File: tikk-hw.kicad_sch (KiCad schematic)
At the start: 148 parts, among them J1 51281-0598, P6 ZX-SH1.0-4PWT, SW1 TS24CA, SW2 TS24CA, U1 IS31FL3731-QFLS2-TR, U2 LIS2DH12TR, U3 Tenstar nRF52840, U4 CP6208DTR(XBLW), U5 TMP102AIDRLR, U6 CP6208DTR(XBLW)

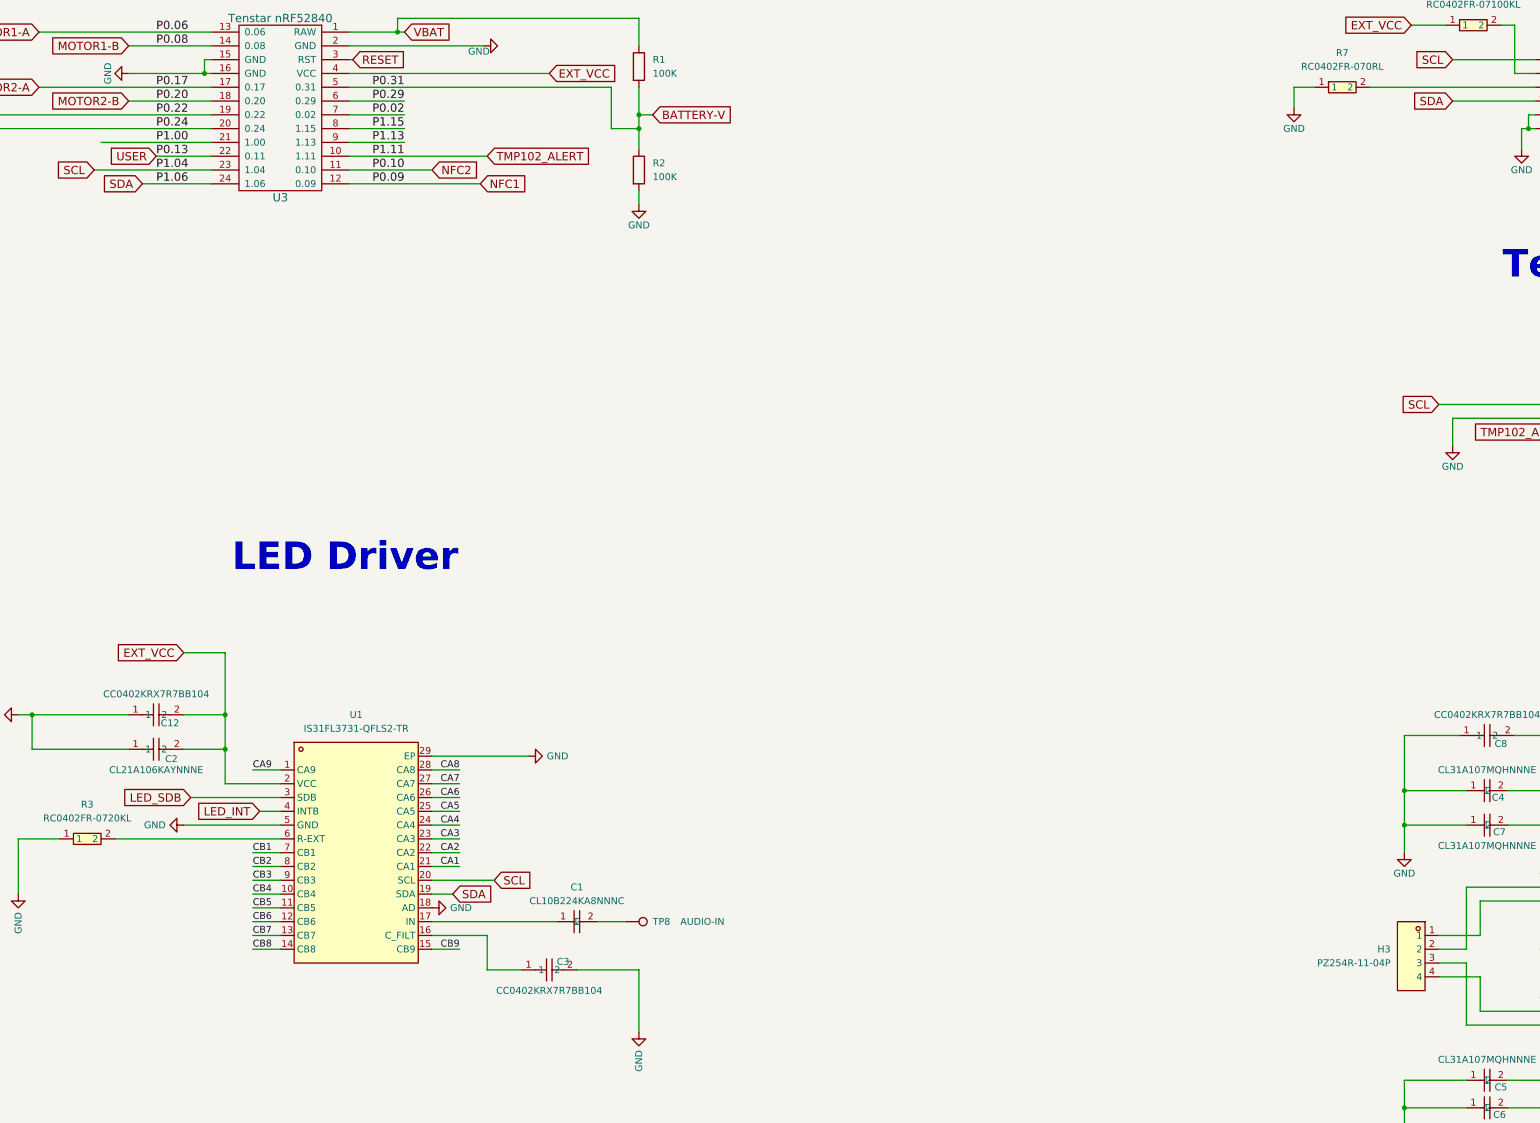
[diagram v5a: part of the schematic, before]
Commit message: Removed all initial DRC violations
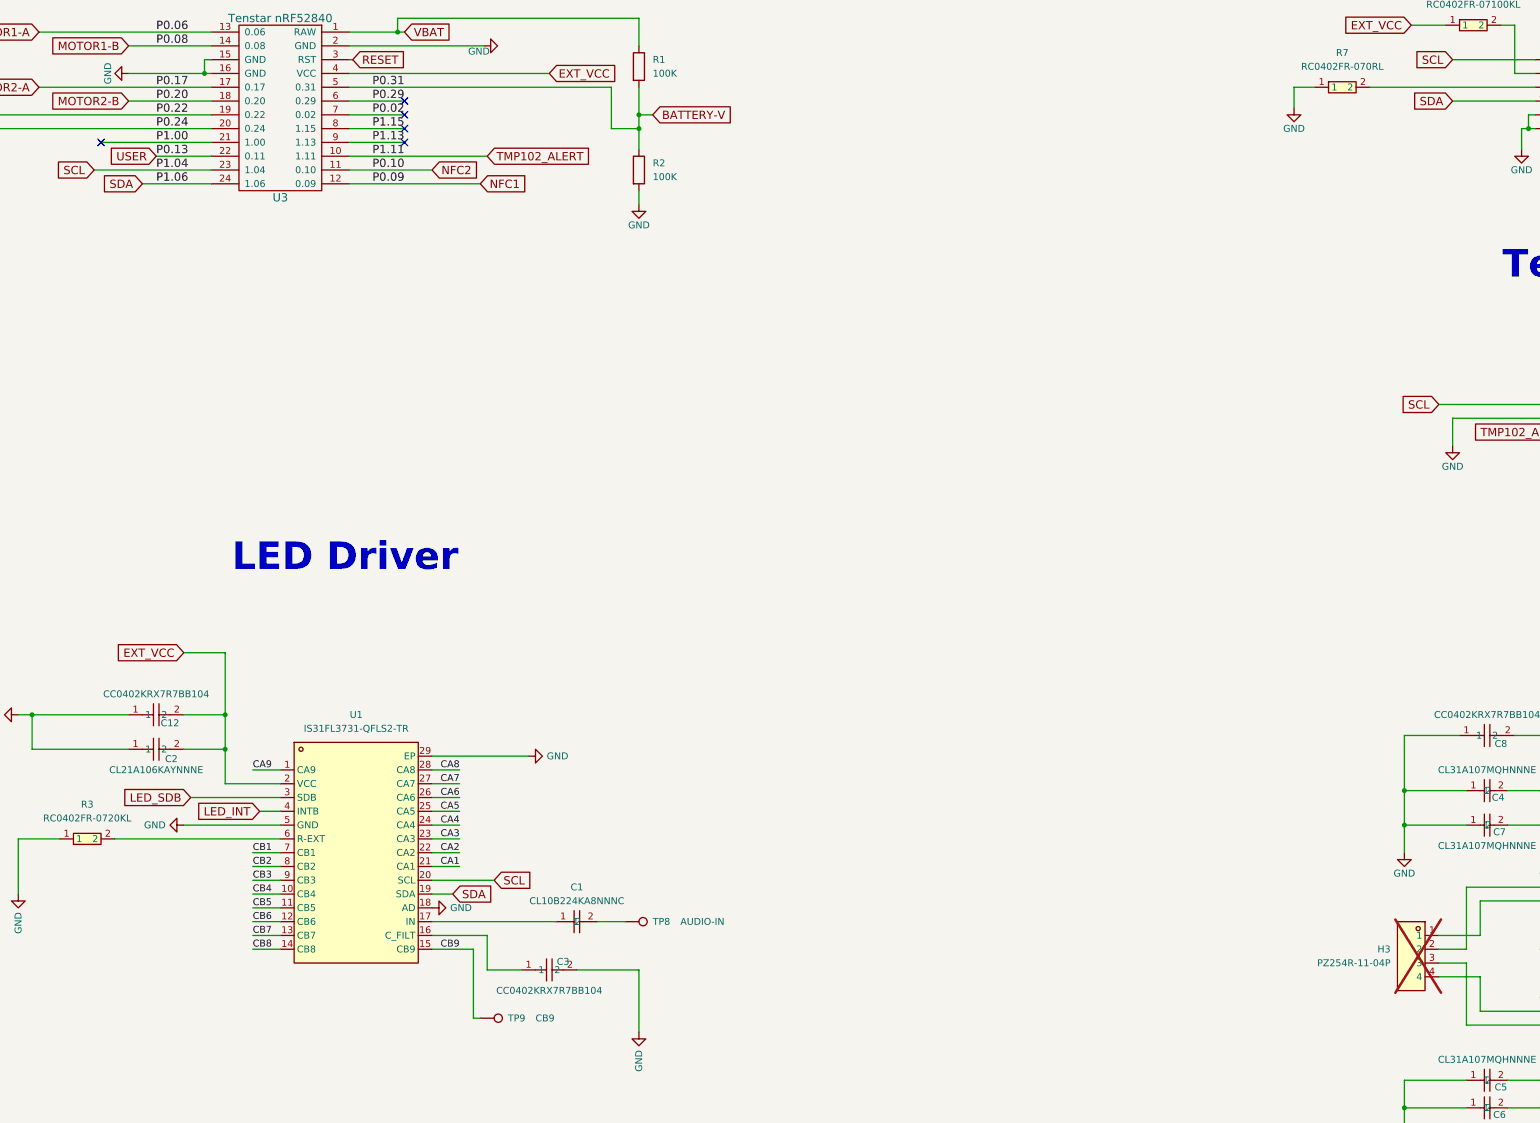
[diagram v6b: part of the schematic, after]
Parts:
- added TP9: CB9, TestPoint:TestPoint_Pad_D1.0mm, symbol Connector:TestPoint
- H3: now not fitted
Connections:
- net CB9: now also TP9.1
- no-connect marks 4 -> 9
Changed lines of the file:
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@@
 	)
 	(no_connect
+		(at 237.49 55.88)
+	)
+	(no_connect
+		(at 237.49 50.8)
+	)
+	(no_connect
 		(at 492.76 195.58)
 	)
 	(no_connect
+		(at 237.49 53.34)
+	)
+	(no_connect
 		(at 77.47 247.65)
 	)
@@
 		(at 77.47 250.19)
 	)
+	(no_connect
+		(at 181.61 55.88)
+	)
+	(no_connect
+		(at 237.49 48.26)
+	)
 	(wire
 		(pts
@@
 	(wire
 		(pts
+			(xy 250.19 204.47) (xy 250.19 217.17)
+		)
+		(stroke
+			(width 0)
+			(type default)
+		)
+	)
+	(wire
+		(pts
 			(xy 474.98 238.76) (xy 480.06 238.76)
 		)
@@
 	(wire
 		(pts
-			(xy 242.57 204.47) (xy 247.65 204.47)
+			(xy 242.57 204.47) (xy 250.19 204.47)
 		)
 		(stroke
@@
 	(wire
 		(pts
+			(xy 250.19 217.17) (xy 251.46 217.17)
+		)
+		(stroke
+			(width 0)
+			(type default)
+		)
+	)
+	(wire
+		(pts
 			(xy 140.97 297.18) (xy 140.97 311.15)
 		)
@@
 		(in_bom yes)
 		(on_board yes)
-		(dnp no)
+		(dnp yes)
 		(property "Reference" "H3"
 			(at 419.1 204.4699 0)
@@
 					(unit 1)
 				)
+			)
+		)
+	)
+	(symbol
+		(lib_id "Connector:TestPoint")
+		(at 251.46 217.17 270)
+		(unit 1)
+		(exclude_from_sim no)
+		(in_bom yes)
+		(on_board yes)
+		(dnp no)
+		(property "Reference" "TP9"
+			(at 256.54 217.17 90)
+			(effects
+				(font
+					(size 1.27 1.27)
+				)
+				(justify left)
+			)
+		)
+		(property "Value" "CB9"
+			(at 261.62 217.17 90)
+			(effects
+				(font
+					(size 1.27 1.27)
+				)
+				(justify left)
+			)
+		)
+		(property "Footprint" "TestPoint:TestPoint_Pad_D1.0mm"
+			(at 251.46 222.25 0)
+			(effects
+				(font
+					(size 1.27 1.27)
+				)
+				(hide yes)
+			)
+		)
+		(property "Datasheet" "~"
+			(at 251.46 222.25 0)
+			(effects
+				(font
+					(size 1.27 1.27)
+				)
+				(hide yes)
+			)
+		)
+		(property "Description" "test point"
+			(at 251.46 217.17 0)
+			(effects
+				(font
+					(size 1.27 1.27)
+				)
+				(hide yes)
+			)
+		)
+		(pin "1"
+		)
+		(instances
+			(project "tikk-hw"
+				(path "/3d32aeaf-a681-4c47-a6d3-68ef8c82b0dd"
+					(reference "TP9")
+					(unit 1)
+				)

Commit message: updated to add silkscreen qr code area and optimized component info
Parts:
- H1, H2, JP1, TP1, TP2, TP3, TP4, TP5, TP6, TP7, TP8, TP9, U3: now not fitted
- R1, R2: value 100K -> RC0402FR-07100KL
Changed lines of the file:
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@@
 			)
 		)
-		(property "Value" "100K"
+		(property "Value" "RC0402FR-07100KL"
 			(at 283.21 62.2299 0)
 			(effects
@@
 		(in_bom yes)
 		(on_board yes)
-		(dnp no)
+		(dnp yes)
 		(property "Reference" "TP8"
 			(at 283.21 199.39 90)
@@
 		(in_bom yes)
 		(on_board yes)
-		(dnp no)
+		(dnp yes)
 		(property "Reference" "TP4"
 			(at 66.04 53.34 90)
@@
 		(in_bom yes)
 		(on_board yes)
-		(dnp no)
+		(dnp yes)
 		(property "Reference" "TP1"
 			(at 65.786 45.72 90)
@@
 		(in_bom yes)
 		(on_board yes)
-		(dnp no)
+		(dnp yes)
 		(property "Reference" "TP3"
 			(at 65.786 50.8 90)
@@
 		(in_bom no)
 		(on_board yes)
-		(dnp no)
+		(dnp yes)
 		(fields_autoplaced yes)
 		(property "Reference" "H1"
@@
 		(in_bom yes)
 		(on_board yes)
-		(dnp no)
+		(dnp yes)
 		(property "Reference" "U3"
 			(at 214.63 66.04 0)
@@
 		(in_bom yes)
 		(on_board yes)
-		(dnp no)
+		(dnp yes)
 		(property "Reference" "TP5"
 			(at 94.996 55.88 90)
@@
 			)
 		)
-		(property "Value" "100K"
+		(property "Value" "RC0402FR-07100KL"
 			(at 283.21 43.1799 0)
 			(effects
@@
 		(in_bom yes)
 		(on_board yes)
-		(dnp no)
+		(dnp yes)
 		(property "Reference" "TP9"
 			(at 256.54 217.17 90)
@@
 		(in_bom yes)
 		(on_board yes)
-		(dnp no)
+		(dnp yes)
 		(property "Reference" "TP7"
 			(at 82.55 250.19 90)
@@
 		(in_bom no)
 		(on_board yes)
-		(dnp no)
+		(dnp yes)
 		(fields_autoplaced yes)
 		(property "Reference" "H2"
@@
 		(in_bom yes)
 		(on_board yes)
-		(dnp no)
+		(dnp yes)
 		(property "Reference" "TP6"
 			(at 82.55 247.65 90)
@@
 		(in_bom no)
 		(on_board yes)
-		(dnp no)
+		(dnp yes)
 		(fields_autoplaced yes)
 		(property "Reference" "JP1"
@@
 		(in_bom yes)
 		(on_board yes)
-		(dnp no)
+		(dnp yes)
 		(property "Reference" "TP2"
 			(at 95.25 48.26 90)

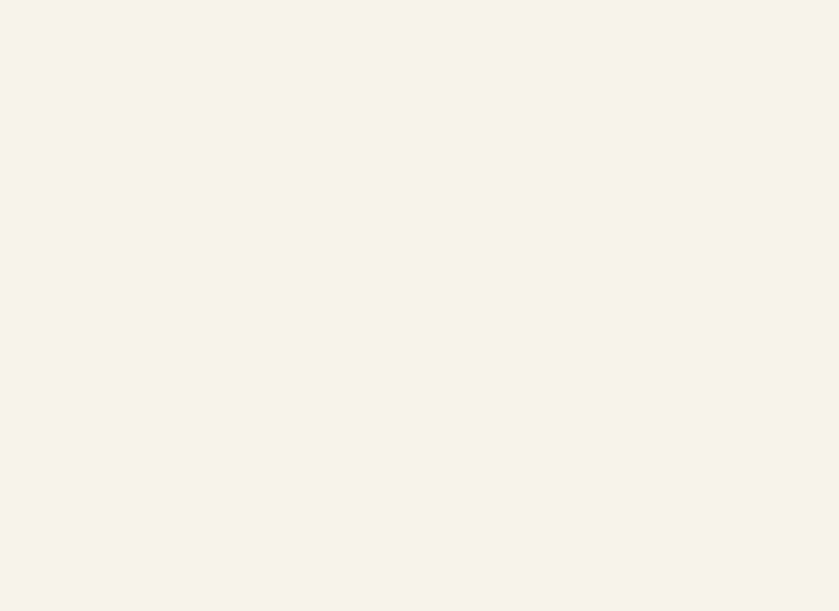
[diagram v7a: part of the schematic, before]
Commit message: add fiducials for mfg
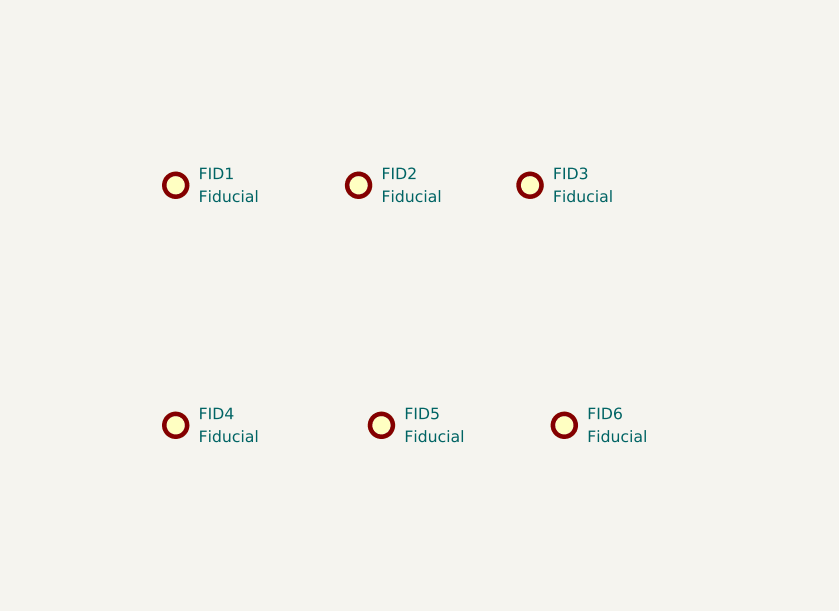
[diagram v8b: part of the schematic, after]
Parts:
- added FID1, FID2, FID3, FID4, FID5, FID6: Fiducial, Fiducial:Fiducial_0.5mm_Mask1mm, symbol Mechanical:Fiducial
